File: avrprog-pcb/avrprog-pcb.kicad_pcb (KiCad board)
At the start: 2 copper layers, 80 x 45.7 mm, 45 parts, among them J1 usb, J2 em_clk, J3 selfprog, J4 prog, U1 FT232RL, U2 ATmega8A-PU, Y1 7.3728MHz

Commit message: designing PCB
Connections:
- U2 pad 25: PRG_MISO -> PRG_MOSI
- U2 pad 26: PRG_SCK -> PRG_RESET
- U2 pad 27: PRG_RESET -> PRG_SCK
- U2 pad 28: PRG_MOSI -> PRG_MISO
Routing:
- net GND: track 0.00 -> 223.1 mm, vias 0 -> 5
- net VCC: track 0.00 -> 152.3 mm, vias 0 -> 1
- net AT_RESET: track 0.00 -> 67.6 mm, vias 0 -> 4
- net AT_MOSI: track 0.00 -> 43.9 mm, vias 0 -> 1
- net Net-(J1-Pad1): track 0.00 -> 40.4 mm, vias 0 -> 1
- net AT_SCK: track 0.00 -> 38.8 mm, vias 0 -> 3
- net AT_TXD: track 0.00 -> 37.2 mm, vias 0 -> 1
- net AT_RXD: track 0.00 -> 36.1 mm, vias 0 -> 1
- net Net-(R3-Pad1): track 0.00 -> 29.3 mm
- net AT_MISO: track 0.00 -> 24.7 mm, vias 0 -> 1
- net Net-(R4-Pad1): track 0.00 -> 22.7 mm
- net PRG_SCK: track 0.00 -> 13.7 mm
- net Net-(R5-Pad1): track 0.00 -> 12.0 mm, vias 0 -> 1
- net PRG_MISO: track 0.00 -> 11.9 mm
- net Net-(C9-Pad1): track 0.00 -> 11.5 mm
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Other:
- net class Default: clearance 0.2 -> 0.3; trace_width 0.25 -> 1; via_dia 0.8 -> 1; via_drill 0.4 -> 0.8
- rule trace_clearance: 0.2 -> 0.3

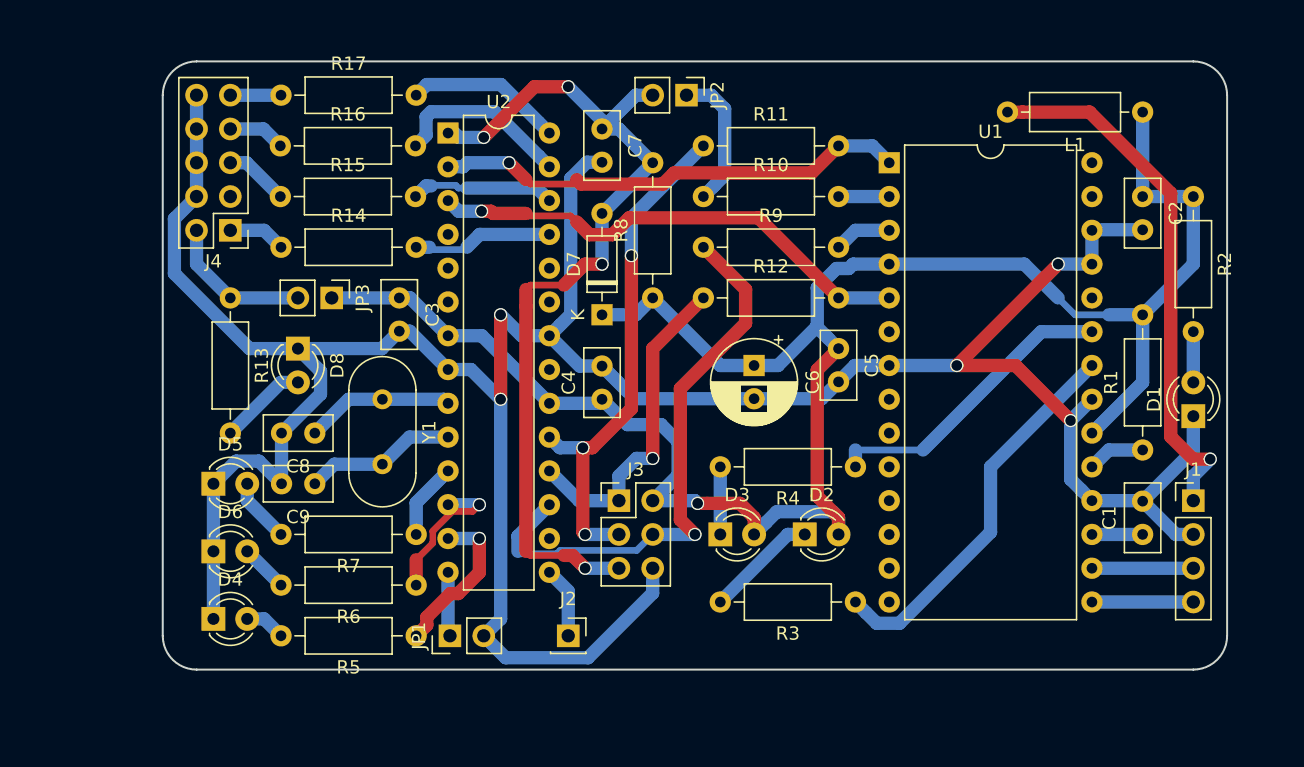
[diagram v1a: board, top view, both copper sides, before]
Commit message: PCB redesigned for smaller size transition from make to meson + ninja
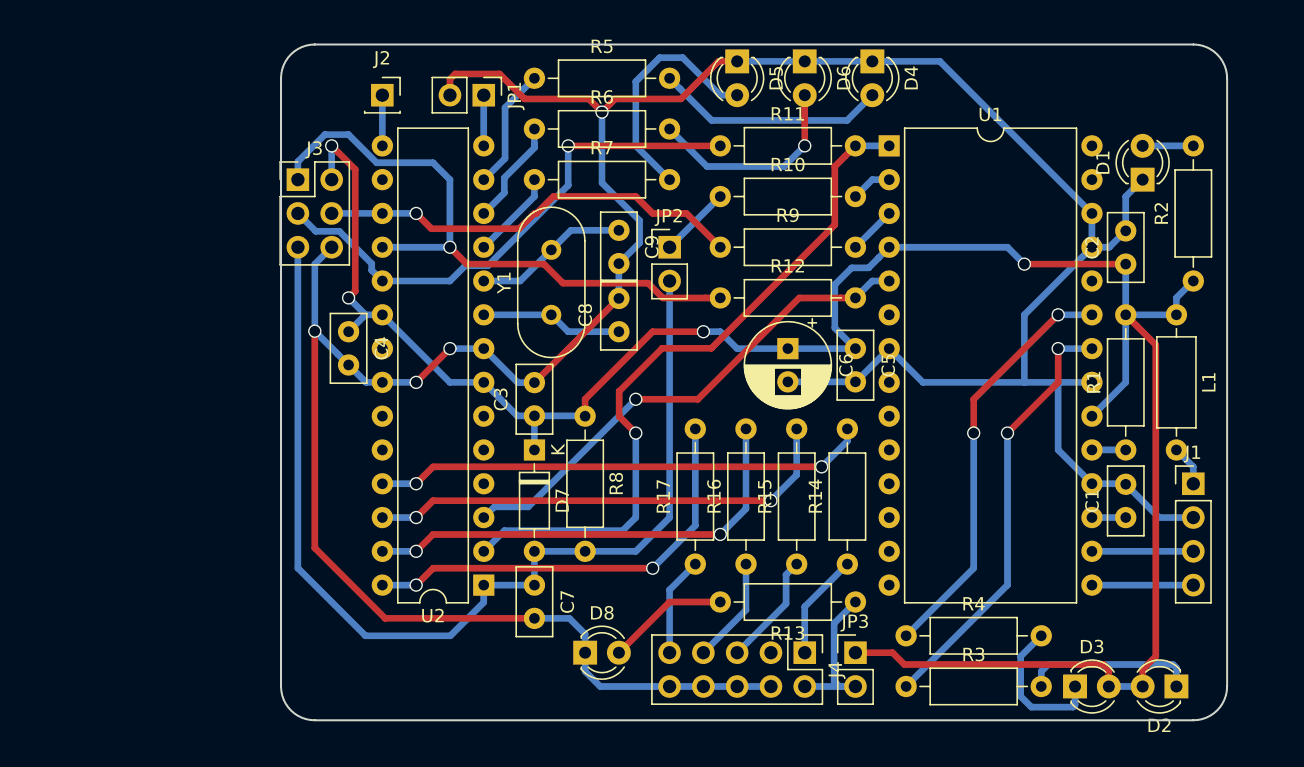
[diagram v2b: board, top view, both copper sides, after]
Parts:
- moved D4 64.9 mm to (151.1, 74.9), turned to 270 degrees
- moved D6 57.7 mm to (146.1, 74.9), turned to 270 degrees
- moved J4 53.6 mm to (146.1, 119.4), turned to 270 degrees
- moved R13 52.3 mm to (149.9, 115.6), turned to 180 degrees
- moved D5 50.6 mm to (141.0, 74.9), turned to 270 degrees
- moved R14 48.8 mm to (149.3, 112.7), turned to 90 degrees
- moved R15 47.6 mm to (145.4, 112.7), turned to 90 degrees
- moved JP3 47.6 mm to (149.9, 119.4), turned to 0 degrees
- moved R16 47.1 mm to (141.6, 112.7), turned to 90 degrees
- moved R17 47.0 mm to (137.8, 112.7), turned to 90 degrees
- moved J2 43.0 mm to (114.3, 77.5)
- moved R5 42.8 mm to (125.7, 76.2), turned to 0 degrees
- moved JP1 40.7 mm to (121.9, 77.5), turned to 270 degrees
- moved R6 35.4 mm to (125.7, 80.0), turned to 0 degrees
- moved C7 34.7 mm to (125.7, 114.3)
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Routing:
- net Net-(J1-Pad1): track 40.4 -> 3.07 mm, vias 1 -> 0
- net PRG_MOSI: track 10.6 -> 37.2 mm, vias 0 -> 2
- net PRG_RESET: track 10.9 -> 35.9 mm, vias 0 -> 2
- net AT_MISO: track 24.7 -> 47.1 mm
- net PRG_SCK: track 13.7 -> 34.7 mm, vias 0 -> 2
- net PRG_MISO: track 11.9 -> 32.6 mm, vias 0 -> 2
- net AT_RXD: track 36.1 -> 53.0 mm
- net Net-(D4-Pad2): track 3.07 -> 17.3 mm
- net VCC: track 152.3 -> 166.0 mm, vias 1 -> 4
- net Net-(D5-Pad2): track 4.86 -> 18.0 mm
- net Net-(D6-Pad2): track 3.59 -> 15.8 mm, vias 0 -> 1
- net AT_MOSI: track 43.9 -> 32.3 mm
- net AT_RESET: track 67.6 -> 77.9 mm, vias 4 -> 0
- net Net-(R4-Pad1): track 22.7 -> 31.4 mm, vias 0 -> 2
- net GND: track 223.1 -> 231.4 mm, vias 5 -> 4
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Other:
- board size 80 x 45.7 mm -> 71.1 x 50.8 mm
- net class Default: clearance 0.3 -> 0.5; trace_width 1 -> 0.5
- rule trace_clearance: 0.3 -> 0.5

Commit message: schematics and PCB mod
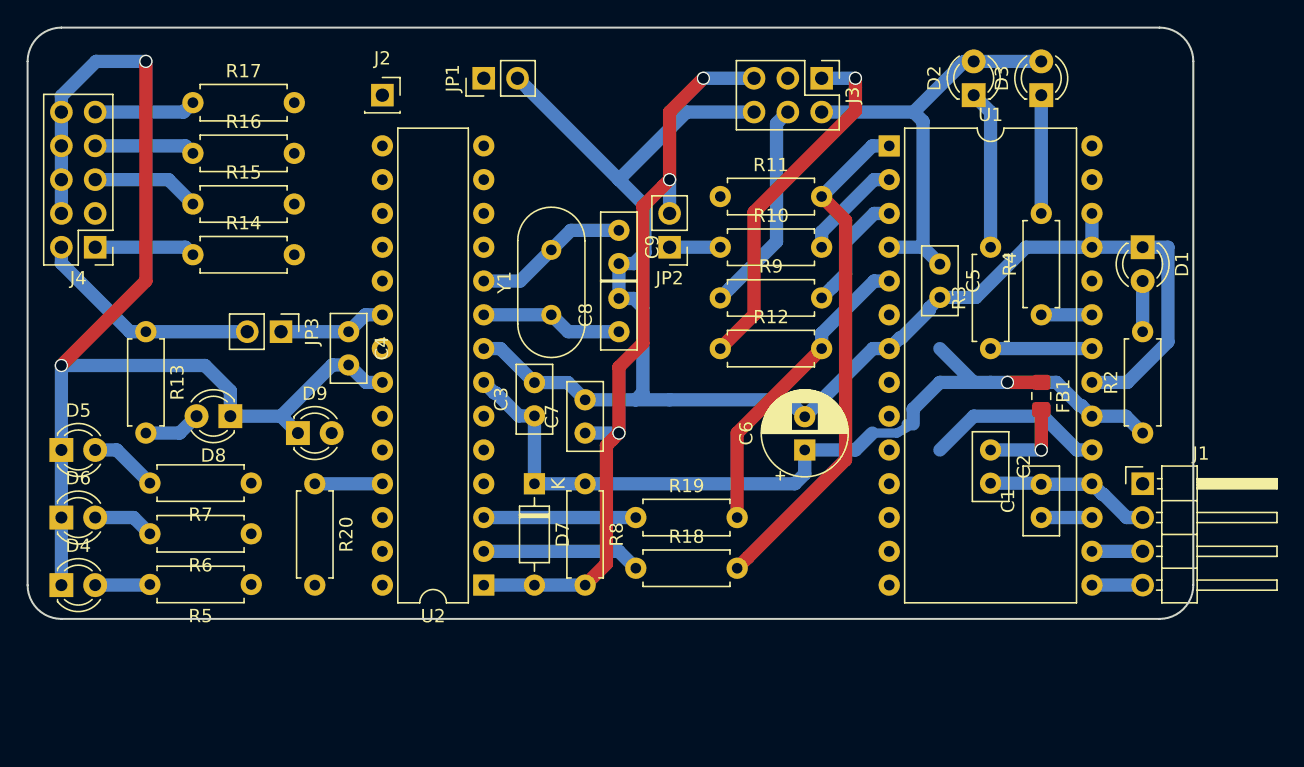
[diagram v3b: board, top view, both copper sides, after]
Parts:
- removed L1: 10mH, Inductor_THT:L_Axial_L6.6mm_D2.7mm_P10.16mm_Horizontal_Vishay_IM-2
- removed R1: 1K, Resistor_THT:R_Axial_DIN0207_L6.3mm_D2.5mm_P10.16mm_Horizontal
- added D9: yellow, TX, LED_THT:LED_D3.0mm, F.Cu at (108.0, 102.9)
- added FB1: ferrite, Inductor_SMD:L_0805_2012Metric_Pad1.15x1.40mm_HandSolder, F.Cu at (163.8, 100.1)
- added R18: 1K, Resistor_THT:R_Axial_DIN0207_L6.3mm_D2.5mm_P7.62mm_Horizontal, F.Cu at (133.3, 113.0)
- added R19: 1K, Resistor_THT:R_Axial_DIN0207_L6.3mm_D2.5mm_P7.62mm_Horizontal, F.Cu at (133.3, 109.2)
- added R20: 1K, Resistor_THT:R_Axial_DIN0207_L6.3mm_D2.5mm_P7.62mm_Horizontal, F.Cu at (109.2, 106.7)
- D4: value red -> green
- D5: value green -> red
- J1: footprint Connector_PinHeader_2.54mm:PinHeader_1x04_P2.54mm_Vertical -> Connector_PinHeader_2.54mm:PinHeader_1x04_P2.54mm_Horizontal
- R10, R11, R12, R13, R14, R15, R16, R17, R2, R3, R4, R5, R6, R7, R8, R9: footprint Resistor_THT:R_Axial_DIN0207_L6.3mm_D2.5mm_P10.16mm_Horizontal -> Resistor_THT:R_Axial_DIN0207_L6.3mm_D2.5mm_P7.62mm_Horizontal
- moved D4 72.6 mm to (90.2, 114.3), turned to 0 degrees
- moved D6 65.6 mm to (90.2, 109.2), turned to 0 degrees
- moved J4 61.4 mm to (92.7, 88.9), turned to 180 degrees
- moved D5 58.6 mm to (90.2, 104.1), turned to 0 degrees
- moved R13 57.1 mm to (96.5, 95.2), turned to 270 degrees
- moved R14 54.4 mm to (100.1, 89.5), turned to 0 degrees
- moved R15 52.8 mm to (100.1, 85.7), turned to 0 degrees
- moved R16 51.8 mm to (100.1, 81.8), turned to 0 degrees
- moved R17 51.3 mm to (100.1, 78.0), turned to 0 degrees
- moved JP3 49.5 mm to (106.7, 95.2), turned to 270 degrees
- moved D2 47.0 mm to (158.8, 77.5), turned to 90 degrees
- moved D3 44.5 mm to (163.8, 77.5), turned to 90 degrees
- moved R5 43.6 mm to (104.4, 114.3), turned to 180 degrees
- moved J3 40.1 mm to (147.3, 76.2), turned to 270 degrees
- moved R6 37.1 mm to (104.4, 110.4), turned to 180 degrees
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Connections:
- C2 pad 1: VCC -> Net-(C2-Pad1)
- J1 pad 1: Net-(J1-Pad1) -> Net-(C2-Pad1)
- R11 pad 2: AT_RXD -> FT_TXD
- R12 pad 2: AT_TXD -> FT_RXD
- U1 pad 1: AT_RXD -> FT_TXD
- U1 pad 5: AT_TXD -> FT_RXD
- U2 pad 11: Net-(R7-Pad1) -> PRG_MISO
- U2 pad 12: Net-(R6-Pad1) -> PRG_MOSI
- U2 pad 13: Net-(R5-Pad1) -> PRG_RESET
- U2 pad 25: PRG_MOSI -> Net-(R20-Pad1)
- U2 pad 26: PRG_RESET -> Net-(R7-Pad1)
- U2 pad 27: PRG_SCK -> Net-(R6-Pad1)
- U2 pad 28: PRG_MISO -> Net-(R5-Pad1)
- U2 pad 6: (no net) -> PRG_SCK
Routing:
- net VCC: track 166.0 -> 109.7 mm, vias 4 -> 1
- net AT_RXD: track 53.0 -> 12.0 mm, vias 1 -> 0
- net AT_SCK: track 40.1 -> 0.00 mm, vias 1 -> 0
- net FT_TXD: track 0.00 -> 38.7 mm
- net PRG_MOSI: track 37.2 -> 0.00 mm, vias 2 -> 0
- net PRG_RESET: track 35.9 -> 0.00 mm, vias 2 -> 0
- net PRG_SCK: track 34.7 -> 0.00 mm, vias 2 -> 0
- net PRG_MISO: track 32.6 -> 0.00 mm, vias 2 -> 0
- net Net-(R4-Pad1): track 31.4 -> 3.81 mm, vias 2 -> 0
- net AT_TXD: track 37.8 -> 11.4 mm, vias 1 -> 0
- net Net-(R3-Pad1): track 32.7 -> 7.62 mm, vias 2 -> 0
- net FT_RXD: track 0.00 -> 23.2 mm
- net AT_MISO: track 47.1 -> 27.1 mm
- net AT_RESET: track 77.9 -> 58.3 mm, vias 0 -> 3
- net AT_MOSI: track 32.3 -> 16.1 mm, vias 1 -> 0
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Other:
- board size 71.1 x 50.8 mm -> 87.6 x 44.5 mm
- net class Default: trace_width 0.5 -> 1

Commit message: schematics and PCB mod connector ISP connector 10 to 6
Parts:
- added R1: 1K, Resistor_THT:R_Axial_DIN0207_L6.3mm_D2.5mm_P7.62mm_Horizontal, F.Cu at (156.2, 104.1)
- C1, C3, C4, C5, C7: footprint Capacitor_THT:C_Disc_D5.0mm_W2.5mm_P2.50mm -> Capacitor_THT:C_Rect_L7.2mm_W2.5mm_P5.00mm_FKS2_FKP2_MKS2_MKP2
- R14, R15, R16, R17: value 1K -> 470
- moved C3 2.56 mm to (125.7, 104.1)
- moved C1 2.54 mm to (163.8, 111.8)
- moved C5 2.54 mm to (156.2, 87.6)
- moved D1 2.54 mm to (171.4, 86.4)
- moved R2 2.54 mm to (171.4, 100.3)
- moved C4 1.80 mm to (110.5, 94.0)
- moved C7 1.27 mm to (129.5, 104.1)
- moved D7 1.27 mm to (125.7, 108.0)
- moved R8 1.27 mm to (129.5, 108.0)
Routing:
- net AT_SCK: track 0.00 -> 53.3 mm, vias 0 -> 2
- net AT_MISO: track 27.1 -> 58.3 mm, vias 1 -> 3
- net PRG_SCK: track 0.00 -> 28.5 mm, vias 0 -> 2
- net AT_MOSI: track 16.1 -> 44.1 mm, vias 0 -> 1
- net PRG_MISO: track 0.00 -> 26.6 mm, vias 0 -> 1
- net VCC: track 109.7 -> 134.7 mm, vias 1 -> 6
- net GND: track 220.6 -> 242.2 mm
- net PRG_MOSI: track 0.00 -> 16.6 mm, vias 0 -> 1
- net PRG_RESET: track 0.00 -> 16.1 mm, vias 0 -> 1
- net Net-(D9-Pad2): track 0.00 -> 12.4 mm
- net AT_RESET: track 58.3 -> 70.6 mm
- net Net-(R5-Pad1): track 0.00 -> 11.3 mm
- net Net-(R7-Pad1): track 0.00 -> 10.9 mm
- net Net-(R6-Pad1): track 0.00 -> 10.4 mm
- net Net-(C2-Pad1): track 6.84 -> 16.5 mm
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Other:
- rule trace_min: 0.2 -> 1
